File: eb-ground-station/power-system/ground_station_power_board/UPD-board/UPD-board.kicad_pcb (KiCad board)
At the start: 2 copper layers, 140.7 x 86.5 mm, 166 parts, among them J1 Conn_01x04, J10 PI 1827486, J2 Conn_01x03, J3 Conn_01x06, J4 Conn_01x06, J5 Conn_01x06, J6 Conn_01x06, J7 PI 1809131, J8 PI 1809131, J9 PI 1827486, Q1 DMN61D8L-LVT, Q10 DMN61D8L-LVT, Q11 SUD50P08-25L-E3, Q12 SUD50P08-25L-E3, Q13 DMN61D8L-LVT, Q14 DMN61D8L-LVT, Q15 DMN61D8L-LVT, Q16 SUD50P08-25L-E3, Q17 SUD50P08-25L-E3, Q18 DMN61D8L-LVT, Q19 SUD50P08-25L-E3, Q2 DMN61D8L-LVT, Q20 SUD50P08-25L-E3, Q3 DMN61D8L-LVT, Q4 SUD50P08-25L-E3, Q5 SUD50P08-25L-E3, Q6 DMN61D8L-LVT, Q7 DMN61D8L-LVT, Q8 DMN61D8L-LVT, Q9 DMN61D8L-LVT, U1 MAX7310ATE, U10 TC4427, U11 TC4427, U12 TC4427, U13 TC4427, U14 TC4427, U15 TC4427, U16 TC4427, U17 TC4427, U18 TC4427, U19 TC4427, U2 MAX7310ATE, U3 MAX7310ATE, U4 MCP9808, U5 ADS1115IDGS, U6 UA78M33, U7 U_RasPi_40pin, U8 TC4427, U9 TC4427

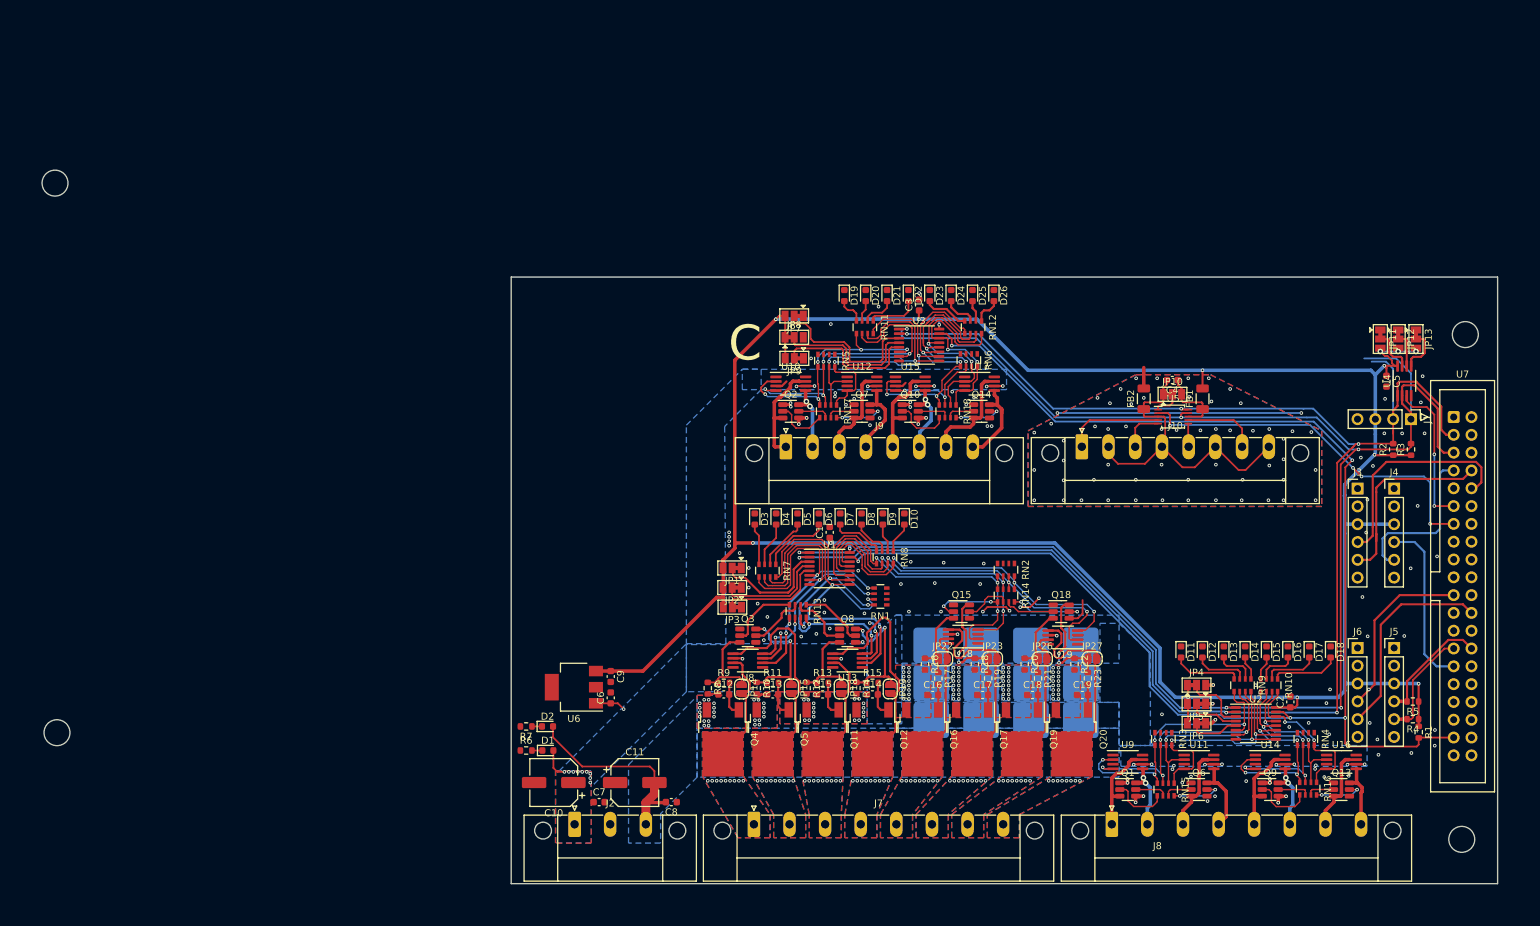
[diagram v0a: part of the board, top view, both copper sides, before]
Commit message: Added PDF schematic
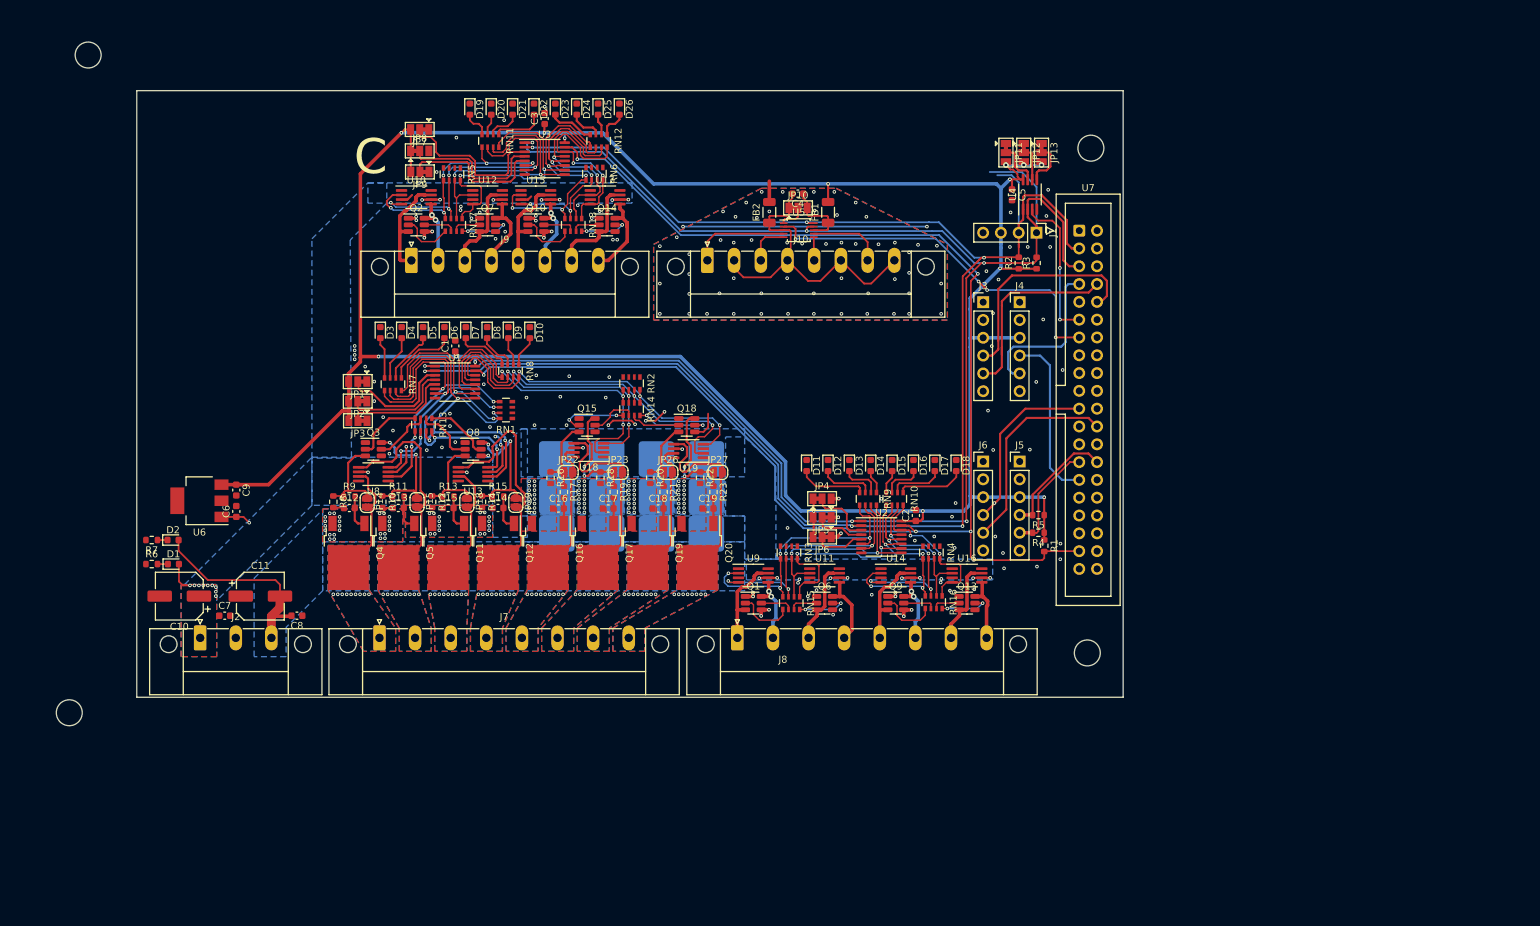
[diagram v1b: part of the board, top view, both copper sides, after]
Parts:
- moved H2 96.8 mm to (67.9, 48.1)
- moved H1 75.6 mm to (65.3, 141.9)
- moved J2 59.7 mm to (83.9, 131.3)
- moved R1 59.7 mm to (204.3, 118.1)
- moved C10 59.7 mm to (80.9, 125.3)
- moved D1 59.7 mm to (80.1, 120.7)
- moved H4 59.7 mm to (210.5, 133.4)
- moved JP14 59.7 mm to (107.7, 112.0)
- moved JP9 59.7 mm to (115.3, 64.8)
- moved C11 59.7 mm to (92.5, 125.3)
- moved C2 59.7 mm to (186.0, 113.8)
- moved C4 59.7 mm to (169.2, 67.9)
- moved C8 59.7 mm to (97.7, 128.1)
- moved D10 59.7 mm to (131.0, 87.7)
- moved D11 59.7 mm to (170.4, 106.7)
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
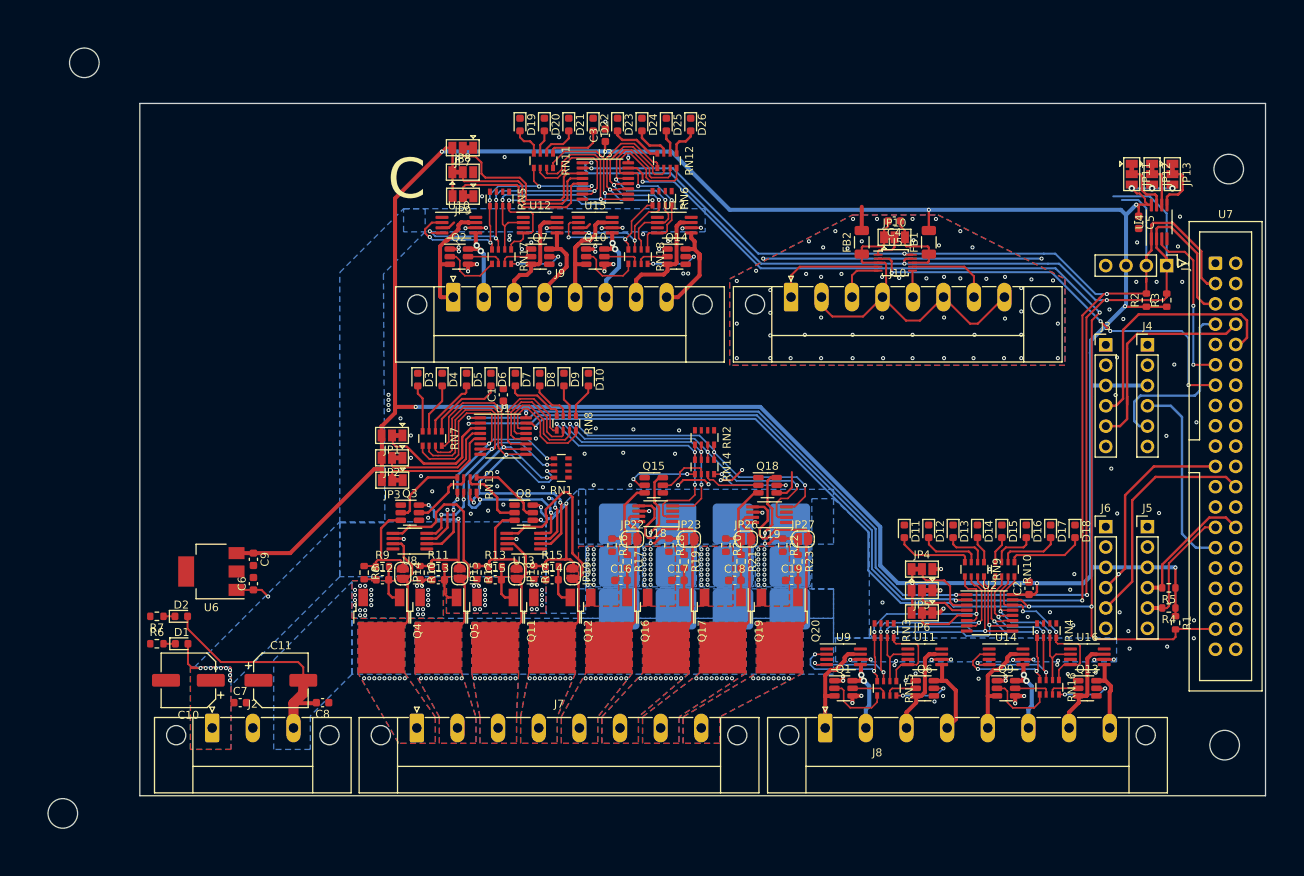
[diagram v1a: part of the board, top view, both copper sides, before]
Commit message: Added soft start and ground vias
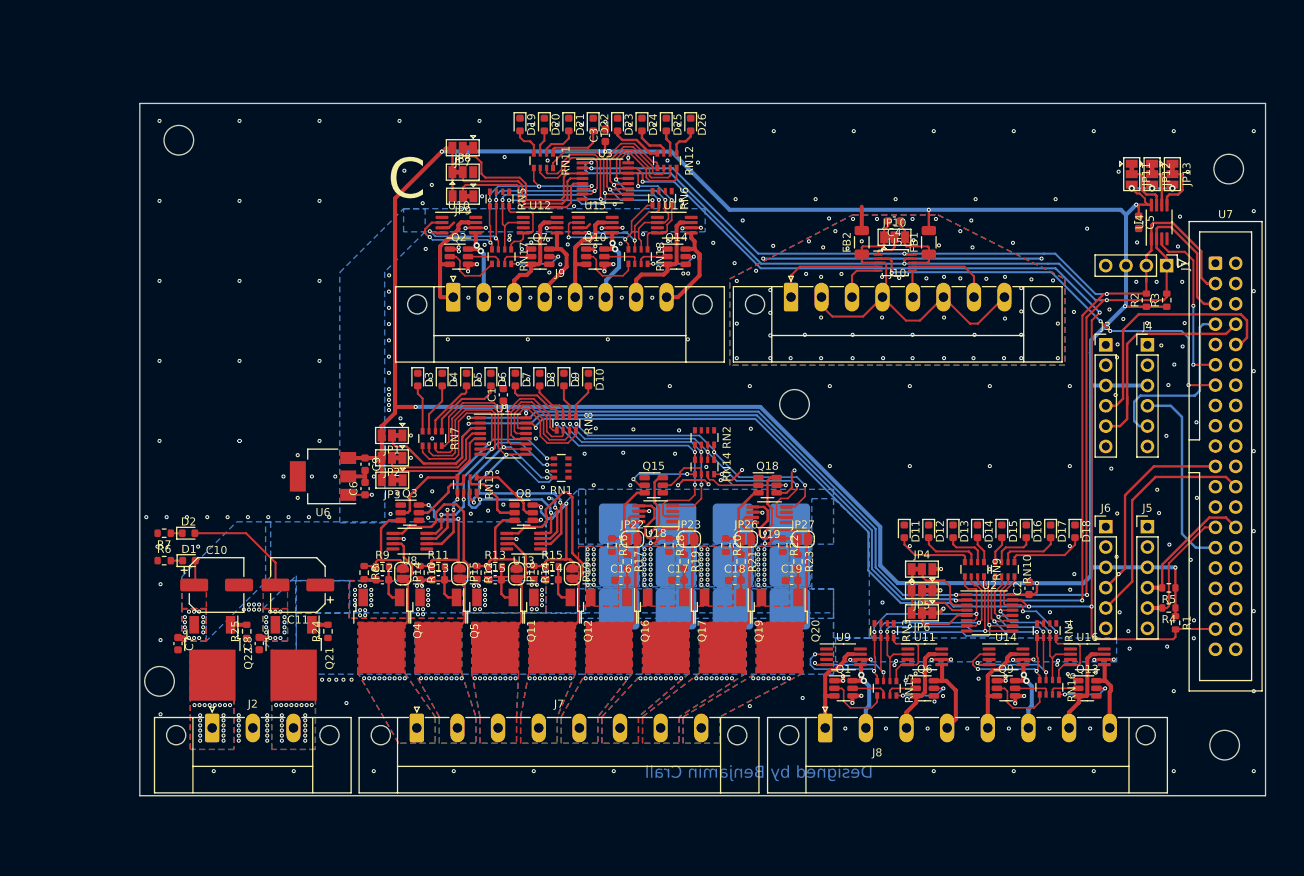
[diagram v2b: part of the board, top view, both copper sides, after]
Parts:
- added ?: , , F.Cu at (156.7, 90.8)
- added Q21: SUD50P08-25L-E3, oresat-footprints:TO-252-3_TabIsPin2, F.Cu at (94.1, 122.6)
- added Q22: SUD50P08-25L-E3, oresat-footprints:TO-252-3_TabIsPin2, F.Cu at (83.9, 122.6)
- added R24: 10k, Resistor_SMD:R_0603_1608Metric, F.Cu at (98.4, 119.2)
- added R25: 10k, Resistor_SMD:R_0603_1608Metric, F.Cu at (88.2, 119.2)
- moved H1 20.5 mm to (77.3, 125.4)
- moved C6 18.3 mm to (103.0, 101.3)
- moved U6 18.3 mm to (97.8, 99.8)
- moved C9 18.3 mm to (103.0, 98.3)
- moved H2 15.3 mm to (79.8, 57.8)
- moved C10 12.4 mm to (84.5, 113.4), turned to 0 degrees
- moved C11 12.1 mm to (94.6, 113.4), turned to 180 degrees
- moved C8 10.8 mm to (89.8, 120.7), turned to 90 degrees
- moved C7 10.7 mm to (79.7, 120.7), turned to -90 degrees
- moved D1 10.4 mm to (81.0, 110.3)
- moved R6 10.4 mm to (77.9, 110.3)
- moved D2 10.4 mm to (81.0, 106.9)
- moved R7 10.4 mm to (77.9, 106.9)
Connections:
- J2 pad 1: +12V -> 12V_RAW
- J2 pad 3: +5V -> 5v_RAW
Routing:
- net +3V3: track 413.6 -> 395.2 mm
- net SCL: track 252.6 -> 238.5 mm
- net +5V: track 32.0 -> 18.1 mm, vias 24 -> 38
- net SDA: track 243.9 -> 233.2 mm
- net GND: track 86.6 -> 90.2 mm, vias 111 -> 302
- net Net-(Q21-Pad1): track 0.00 -> 2.01 mm
- net Net-(Q22-Pad1): track 0.00 -> 2.01 mm
- net +12V: track 32.4 -> 30.6 mm, vias 45 -> 50
- net 5v_RAW: vias 0 -> 20
- net 12V_RAW: vias 0 -> 20
- added copper zone on B.Cu, net 12V_RAW
- added copper zone on F.Cu, net 12V_RAW
- added copper zone on B.Cu, net 5v_RAW
- added copper zone on F.Cu, net 5v_RAW
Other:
- board text added: "Designed by Benjamin Crall"

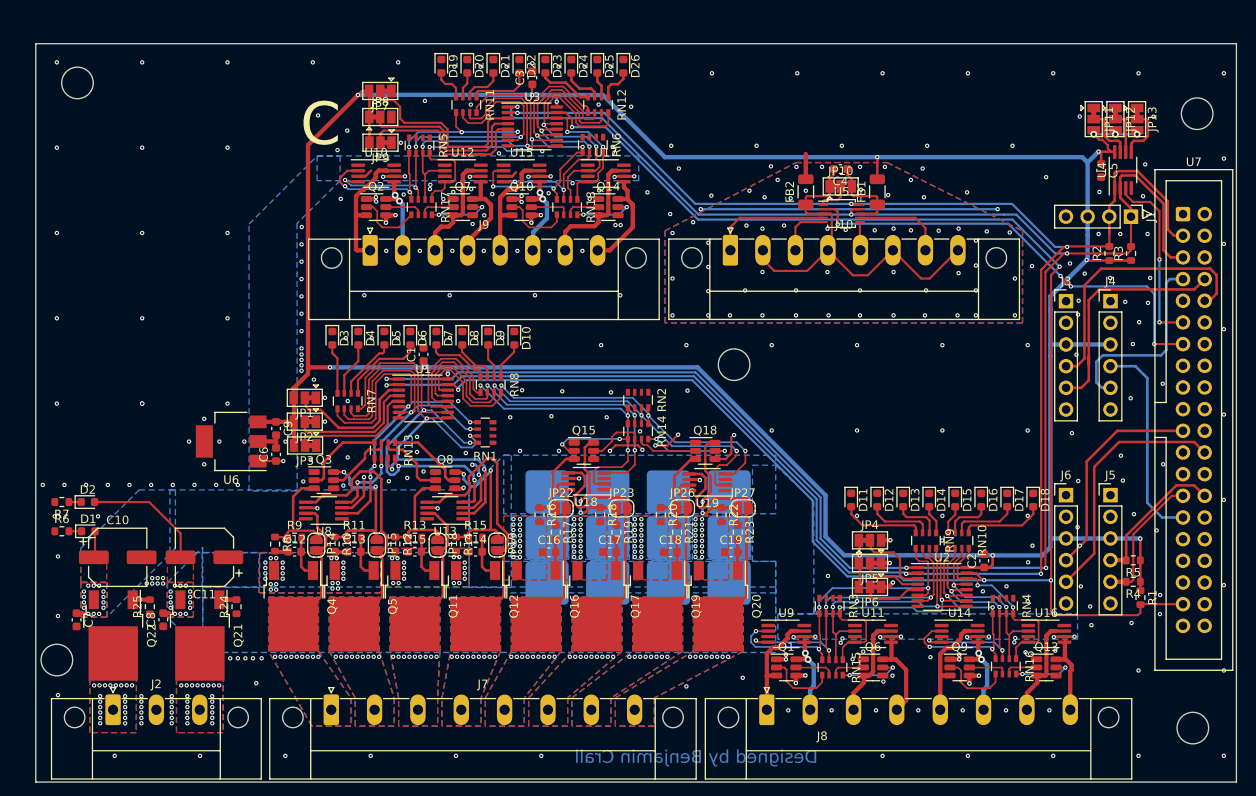
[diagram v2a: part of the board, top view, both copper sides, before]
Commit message: Fixed some silkscreen
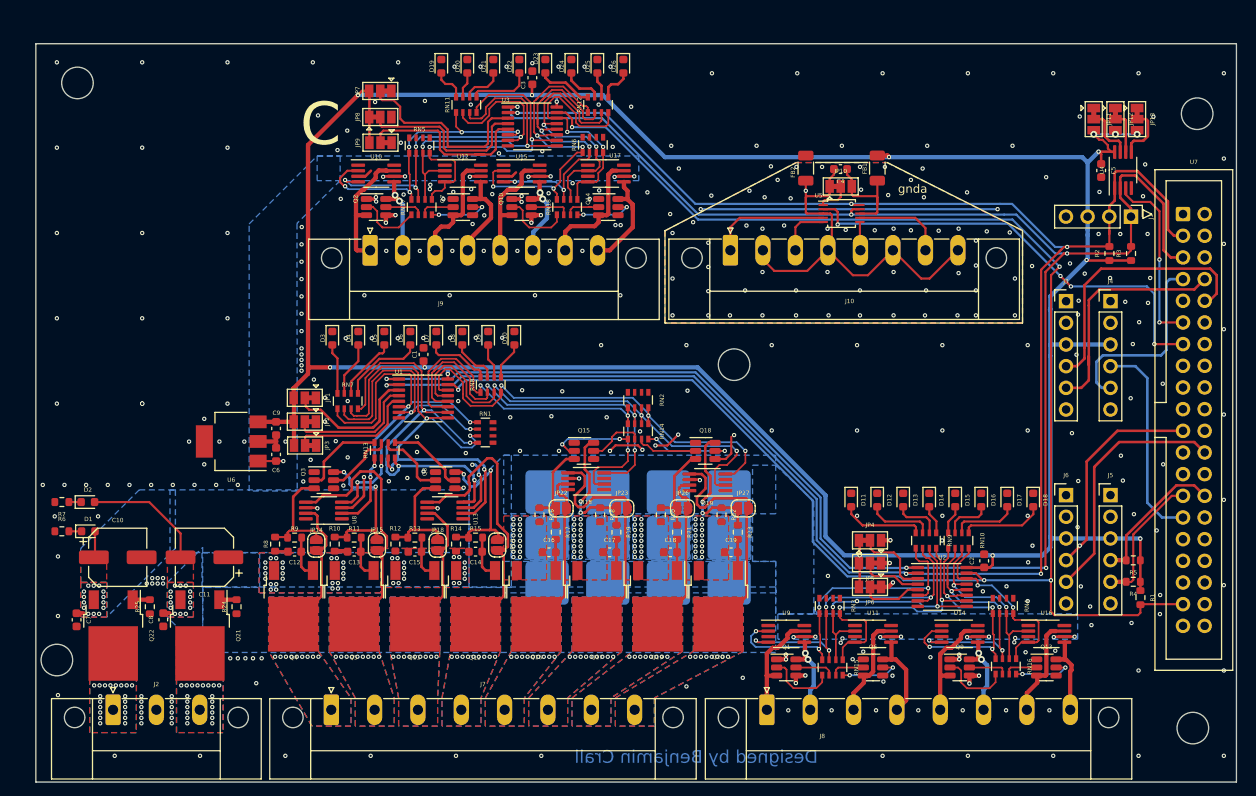
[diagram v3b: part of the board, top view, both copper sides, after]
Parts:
- moved FB1 2.78 mm to (173.5, 67.8)
- moved FB2 2.78 mm to (165.1, 67.8)
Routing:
- net GND: track 90.2 -> 87.2 mm
- net Net-(C4-Pad1): track 10.2 -> 13.0 mm
- net GNDA: track 46.0 -> 48.6 mm
- net +3V3: track 395.2 -> 394.0 mm
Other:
- board text added: "gnda"

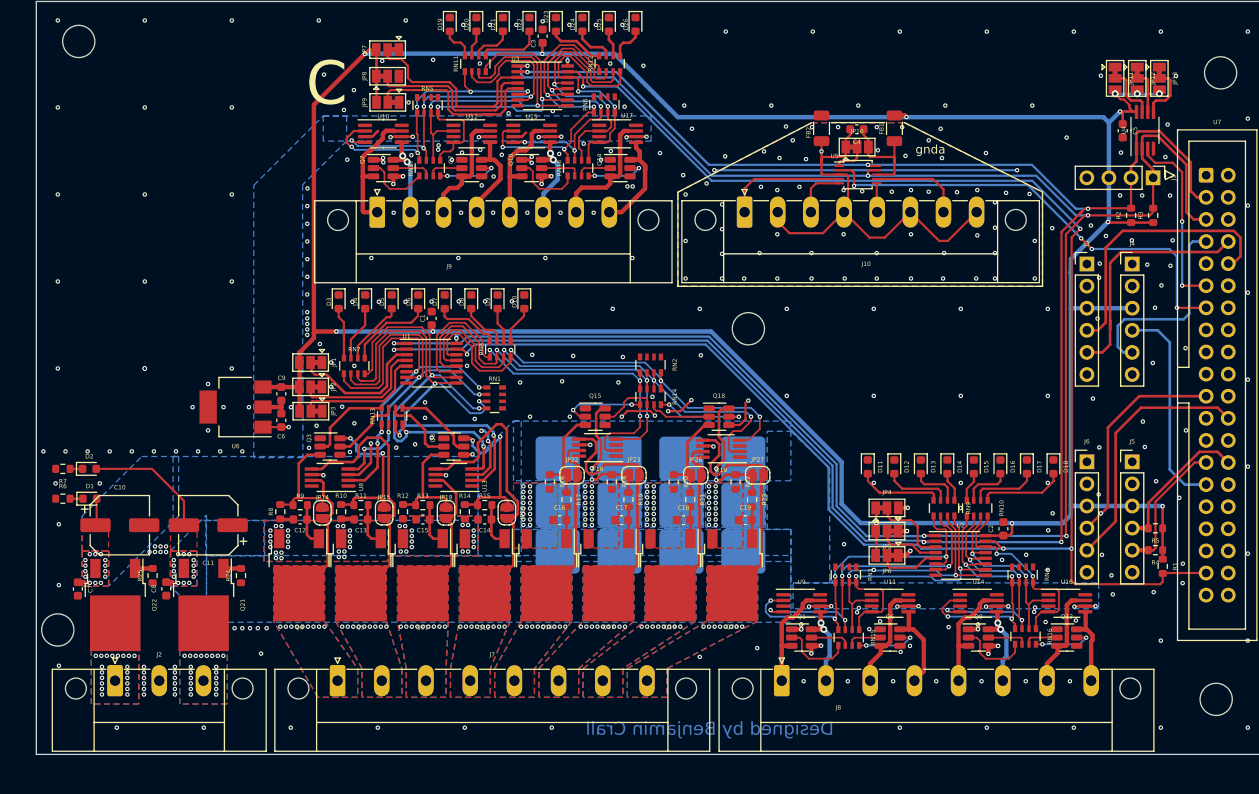
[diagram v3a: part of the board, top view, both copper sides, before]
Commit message: refdes silkscreen nearly done
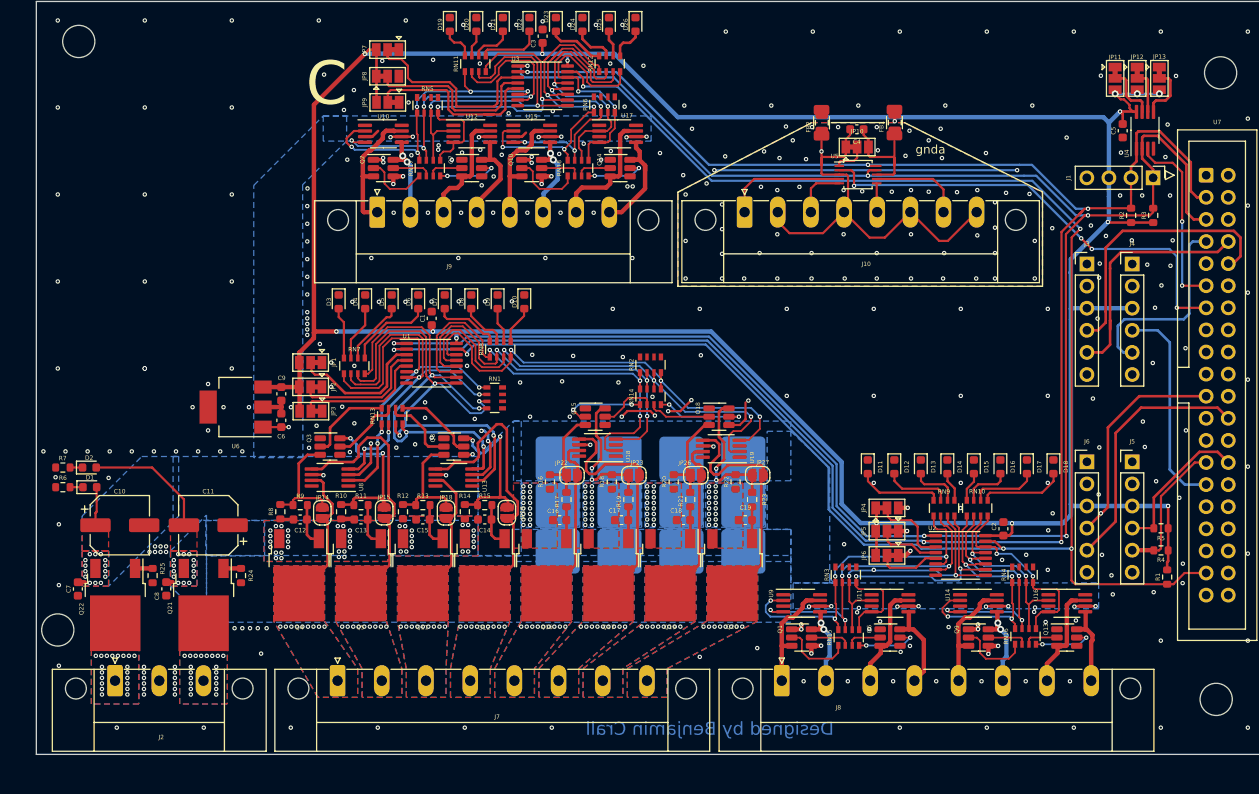
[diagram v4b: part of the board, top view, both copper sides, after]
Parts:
- removed ?: , 
- FB1, FB2: footprint Capacitor_SMD:C_1206_3216Metric -> oresat-footprints:1206-or-0805
- moved R1 1.33 mm to (204.9, 119.3)
- moved D1 1.32 mm to (81.0, 109.0)
- moved R6 1.32 mm to (77.9, 109.0)
- moved FB1 0.66 mm to (173.5, 67.1)
- moved FB2 0.64 mm to (165.1, 67.1)
- moved R4 0.64 mm to (204.1, 116.3)
- moved R5 0.64 mm to (204.1, 113.7)
- moved D2 0.15 mm to (81.0, 106.8)
- moved R7 0.15 mm to (77.9, 106.8)
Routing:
- net +3V3: track 394.0 -> 395.7 mm
- net +12V: track 30.6 -> 32.1 mm
